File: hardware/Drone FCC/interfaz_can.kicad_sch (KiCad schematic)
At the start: 14 parts, among them J15 CAN 1 Connector 1, J16 CAN 2 Connector 1, U1 SN65HVD230, U2 SN65HVD230

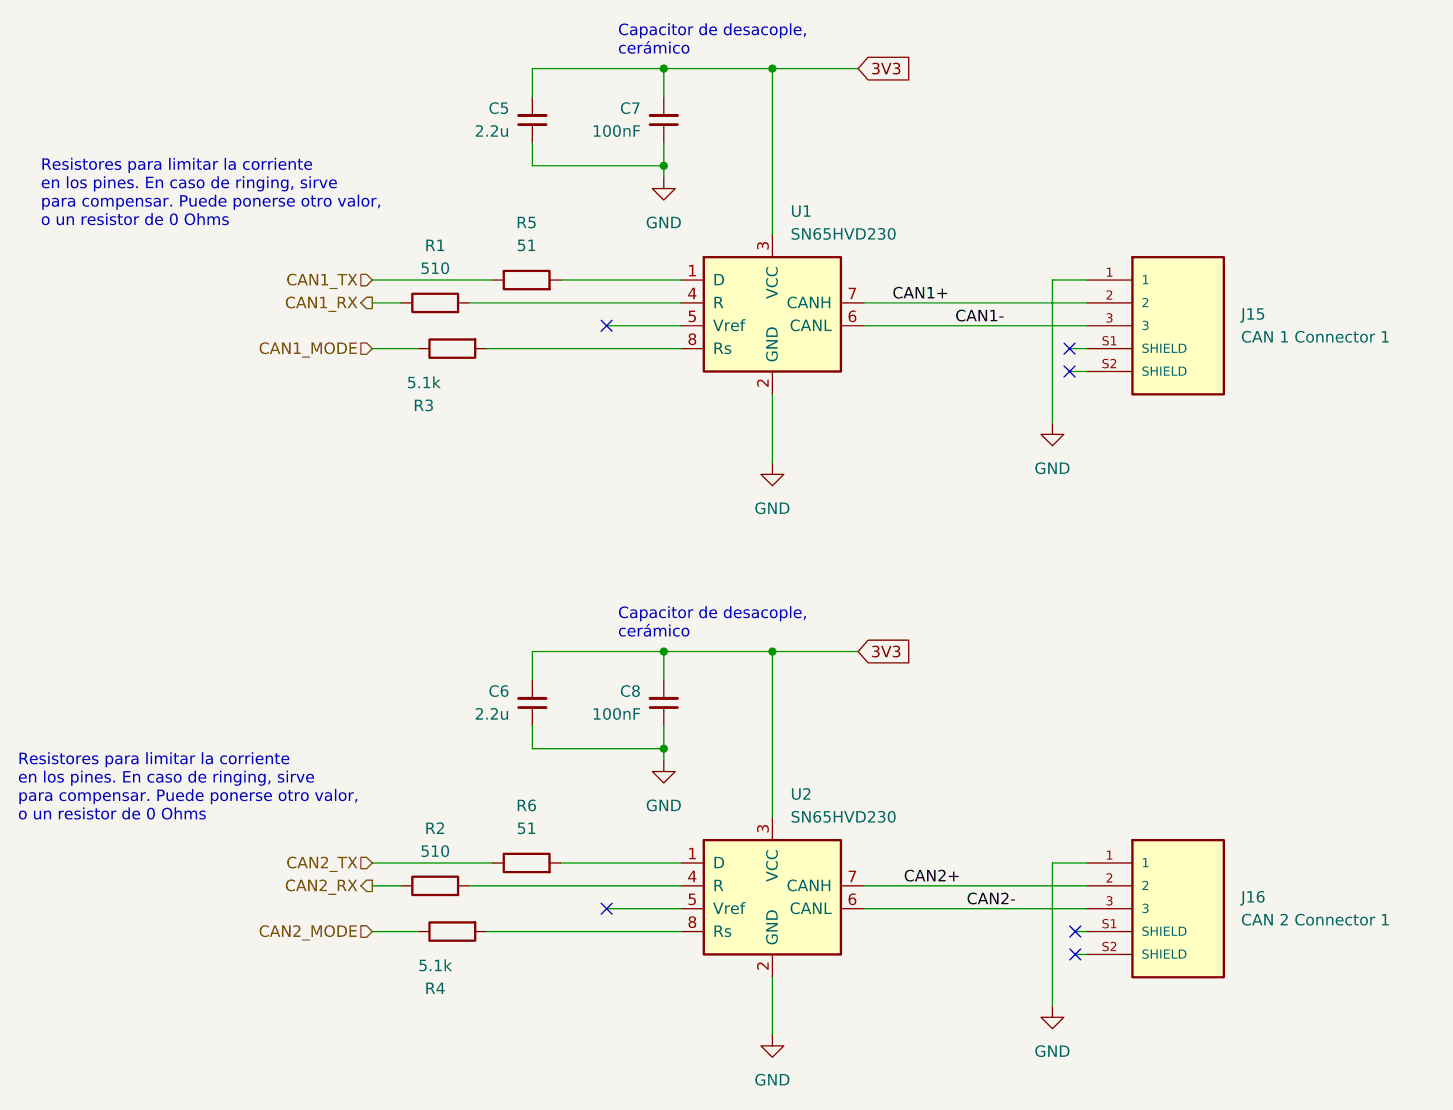
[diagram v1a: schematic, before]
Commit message: connected CAN transcievers slope control pin resistor to gnd
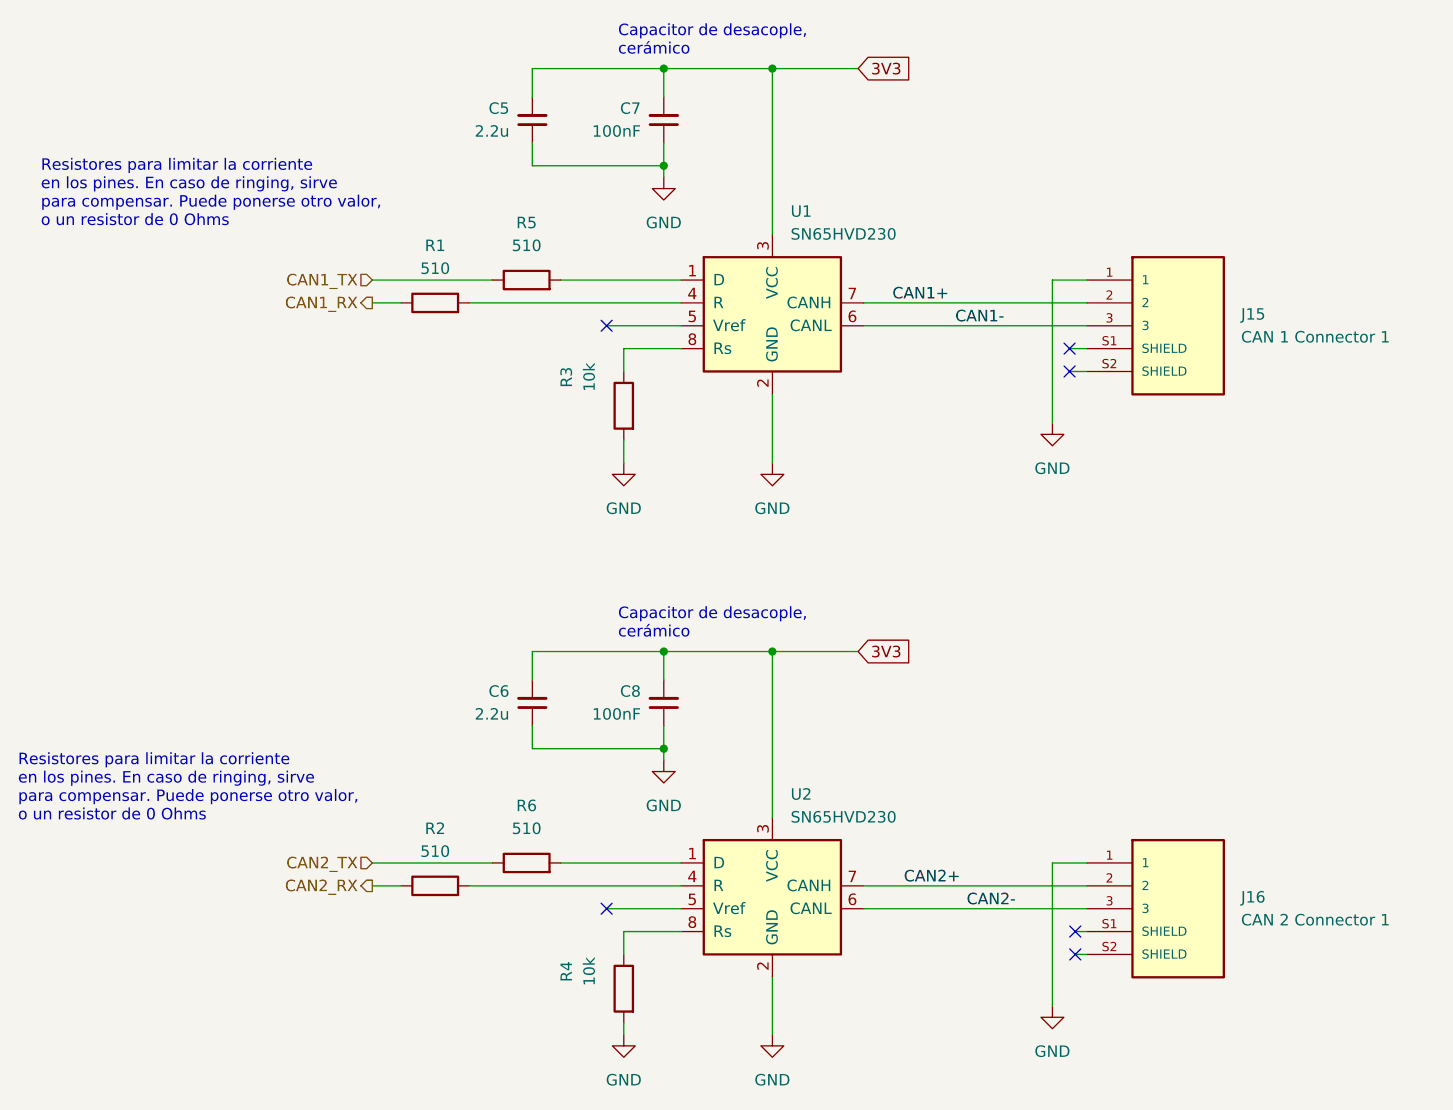
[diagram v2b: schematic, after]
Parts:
- R3, R4: value 5.1k -> 10k
- R5, R6: value 51 -> 510
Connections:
- net CAN1_MODE is gone; now on an unnamed net: R3.1
- net CAN2_MODE is gone; now on an unnamed net: R4.1
- net GND: now also R3.2, R4.2
- net at U1.8 (Rs): no longer R3.2
- net at U2.8 (Rs): no longer R4.2
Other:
- moved on the sheet: R3, R4
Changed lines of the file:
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@@
+    (stroke (width 0) (type default) (color 0 0 0 0))
+  )
+  (wire (pts (xy 128.905 57.15) (xy 135.255 57.15))
     (stroke (width 0) (type default) (color 0 0 0 0))
   )
@@
     (stroke (width 0) (type default) (color 0 0 0 0))
   )
-  (wire (pts (xy 100.965 121.92) (xy 106.045 121.92))
-    (stroke (width 0) (type default) (color 0 0 0 0))
-  )
   (wire (pts (xy 178.435 57.15) (xy 180.34 57.15))
     (stroke (width 0) (type default) (color 0 0 0 0))
@@
     (stroke (width 0) (type default) (color 0 0 0 0))
   )
-  (wire (pts (xy 113.665 57.15) (xy 135.255 57.15))
-    (stroke (width 0) (type default) (color 0 0 0 0))
-  )
-  (wire (pts (xy 113.665 121.92) (xy 135.255 121.92))
-    (stroke (width 0) (type default) (color 0 0 0 0))
-  )
   (wire (pts (xy 155.575 116.84) (xy 180.34 116.84))
     (stroke (width 0) (type default) (color 0 0 0 0))
   )
+  (wire (pts (xy 128.905 67.31) (xy 128.905 69.85))
+    (stroke (width 0) (type default) (color 0 0 0 0))
+  )
   (wire (pts (xy 155.575 54.61) (xy 180.34 54.61))
     (stroke (width 0) (type default) (color 0 0 0 0))
@@
     (stroke (width 0) (type default) (color 0 0 0 0))
   )
-  (wire (pts (xy 100.965 57.15) (xy 106.045 57.15))
-    (stroke (width 0) (type default) (color 0 0 0 0))
-  )
   (wire (pts (xy 133.35 90.805) (xy 133.35 93.98))
     (stroke (width 0) (type default) (color 0 0 0 0))
@@
     (stroke (width 0) (type default) (color 0 0 0 0))
   )
+  (wire (pts (xy 135.255 121.92) (xy 128.905 121.92))
+    (stroke (width 0) (type default) (color 0 0 0 0))
+  )
   (wire (pts (xy 145.415 127) (xy 145.415 133.35))
     (stroke (width 0) (type default) (color 0 0 0 0))
@@
     (stroke (width 0) (type default) (color 0 0 0 0))
   )
+  (wire (pts (xy 128.905 57.15) (xy 128.905 59.69))
+    (stroke (width 0) (type default) (color 0 0 0 0))
+  )
   (wire (pts (xy 127 54.61) (xy 135.255 54.61))
     (stroke (width 0) (type default) (color 0 0 0 0))
@@
     (stroke (width 0) (type default) (color 0 0 0 0))
   )
+  (wire (pts (xy 128.905 132.08) (xy 128.905 133.35))
+    (stroke (width 0) (type default) (color 0 0 0 0))
+  )
   (wire (pts (xy 176.53 114.3) (xy 180.34 114.3))
     (stroke (width 0) (type default) (color 0 0 0 0))
@@
   )
   (wire (pts (xy 179.07 121.92) (xy 180.34 121.92))
+    (stroke (width 0) (type default) (color 0 0 0 0))
+  )
+  (wire (pts (xy 128.905 121.92) (xy 128.905 124.46))
     (stroke (width 0) (type default) (color 0 0 0 0))
   )
@@
     (effects (font (size 1.27 1.27)) (justify right))
   )
-  (hierarchical_label "CAN2_MODE" (shape input) (at 100.965 121.92 180)
-    (effects (font (size 1.27 1.27)) (justify right))
-  )
-  (hierarchical_label "CAN1_MODE" (shape input) (at 100.965 57.15 180)
-    (effects (font (size 1.27 1.27)) (justify right))
-  )
   (symbol (lib_id "Device:R") (at 118.11 114.3 90) (unit 1)
     (in_bom yes) (on_board yes) (fields_autoplaced)
     (property "Reference" "R6" (id 0) (at 118.11 107.95 90))
-    (property "Value" "51" (id 1) (at 118.11 110.49 90))
+    (property "Value" "510" (id 1) (at 118.11 110.49 90))
     (property "Footprint" "Resistor_SMD:R_0402_1005Metric_Pad0.72x0.64mm_HandSolder" (id 2) (at 118.11 116.078 90)
       (effects (font (size 1.27 1.27)) hide)
@@
     (pin "2")
   )
-  (symbol (lib_id "Device:R") (at 109.855 121.92 90) (mirror x) (unit 1)
+  (symbol (lib_id "Device:R") (at 128.905 128.27 0) (mirror y) (unit 1)
     (in_bom yes) (on_board yes)
-    (property "Reference" "R4" (id 0) (at 107.95 128.27 90))
-    (property "Value" "5.1k" (id 1) (at 107.95 125.73 90))
-    (property "Footprint" "Resistor_SMD:R_0402_1005Metric_Pad0.72x0.64mm_HandSolder" (id 2) (at 109.855 120.142 90)
-      (effects (font (size 1.27 1.27)) hide)
-    )
-    (property "Datasheet" "~" (id 3) (at 109.855 121.92 0)
+    (property "Reference" "R4" (id 0) (at 122.555 126.365 90))
+    (property "Value" "10k" (id 1) (at 125.095 126.365 90))
+    (property "Footprint" "Resistor_SMD:R_0402_1005Metric_Pad0.72x0.64mm_HandSolder" (id 2) (at 130.683 128.27 90)
+      (effects (font (size 1.27 1.27)) hide)
+    )
+    (property "Datasheet" "~" (id 3) (at 128.905 128.27 0)
       (effects (font (size 1.27 1.27)) hide)
     )
@@
     (pin "2")
   )
-  (symbol (lib_id "Device:R") (at 109.855 57.15 90) (mirror x) (unit 1)
+  (symbol (lib_id "power:GND") (at 128.905 69.85 0) (unit 1)
+    (in_bom yes) (on_board yes) (fields_autoplaced)
+    (property "Reference" "#PWR0102" (id 0) (at 128.905 76.2 0)
+      (effects (font (size 1.27 1.27)) hide)
+    )
+    (property "Value" "GND" (id 1) (at 128.905 74.93 0))
+    (property "Footprint" "" (id 2) (at 128.905 69.85 0)
+      (effects (font (size 1.27 1.27)) hide)
+    )
+    (property "Datasheet" "" (id 3) (at 128.905 69.85 0)
+      (effects (font (size 1.27 1.27)) hide)
+    )
+    (pin "1")
+  )
+  (symbol (lib_id "Device:R") (at 128.905 63.5 0) (mirror y) (unit 1)
     (in_bom yes) (on_board yes)
-    (property "Reference" "R3" (id 0) (at 106.68 63.5 90))
-    (property "Value" "5.1k" (id 1) (at 106.68 60.96 90))
-    (property "Footprint" "Resistor_SMD:R_0402_1005Metric_Pad0.72x0.64mm_HandSolder" (id 2) (at 109.855 55.372 90)
-      (effects (font (size 1.27 1.27)) hide)
-    )
-    (property "Datasheet" "~" (id 3) (at 109.855 57.15 0)
+    (property "Reference" "R3" (id 0) (at 122.555 60.325 90))
+    (property "Value" "10k" (id 1) (at 125.095 60.325 90))
+    (property "Footprint" "Resistor_SMD:R_0402_1005Metric_Pad0.72x0.64mm_HandSolder" (id 2) (at 130.683 63.5 90)
+      (effects (font (size 1.27 1.27)) hide)
+    )
+    (property "Datasheet" "~" (id 3) (at 128.905 63.5 0)
       (effects (font (size 1.27 1.27)) hide)
     )
@@
     (pin "2")
   )
+  (symbol (lib_id "power:GND") (at 128.905 133.35 0) (unit 1)
+    (in_bom yes) (on_board yes) (fields_autoplaced)
+    (property "Reference" "#PWR0101" (id 0) (at 128.905 139.7 0)
+      (effects (font (size 1.27 1.27)) hide)
+    )
+    (property "Value" "GND" (id 1) (at 128.905 138.43 0))
+    (property "Footprint" "" (id 2) (at 128.905 133.35 0)
+      (effects (font (size 1.27 1.27)) hide)
+    )
+    (property "Datasheet" "" (id 3) (at 128.905 133.35 0)
+      (effects (font (size 1.27 1.27)) hide)
+    )
+    (pin "1")
+  )
   (symbol (lib_id "power:GND") (at 145.415 69.85 0) (unit 1)
     (in_bom yes) (on_board yes) (fields_autoplaced)
@@
     (in_bom yes) (on_board yes) (fields_autoplaced)
     (property "Reference" "R5" (id 0) (at 118.11 43.18 90))
-    (property "Value" "51" (id 1) (at 118.11 45.72 90))
+    (property "Value" "510" (id 1) (at 118.11 45.72 90))
     (property "Footprint" "Resistor_SMD:R_0402_1005Metric_Pad0.72x0.64mm_HandSolder" (id 2) (at 118.11 51.308 90)
       (effects (font (size 1.27 1.27)) hide)

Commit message: updated BOM with passive components
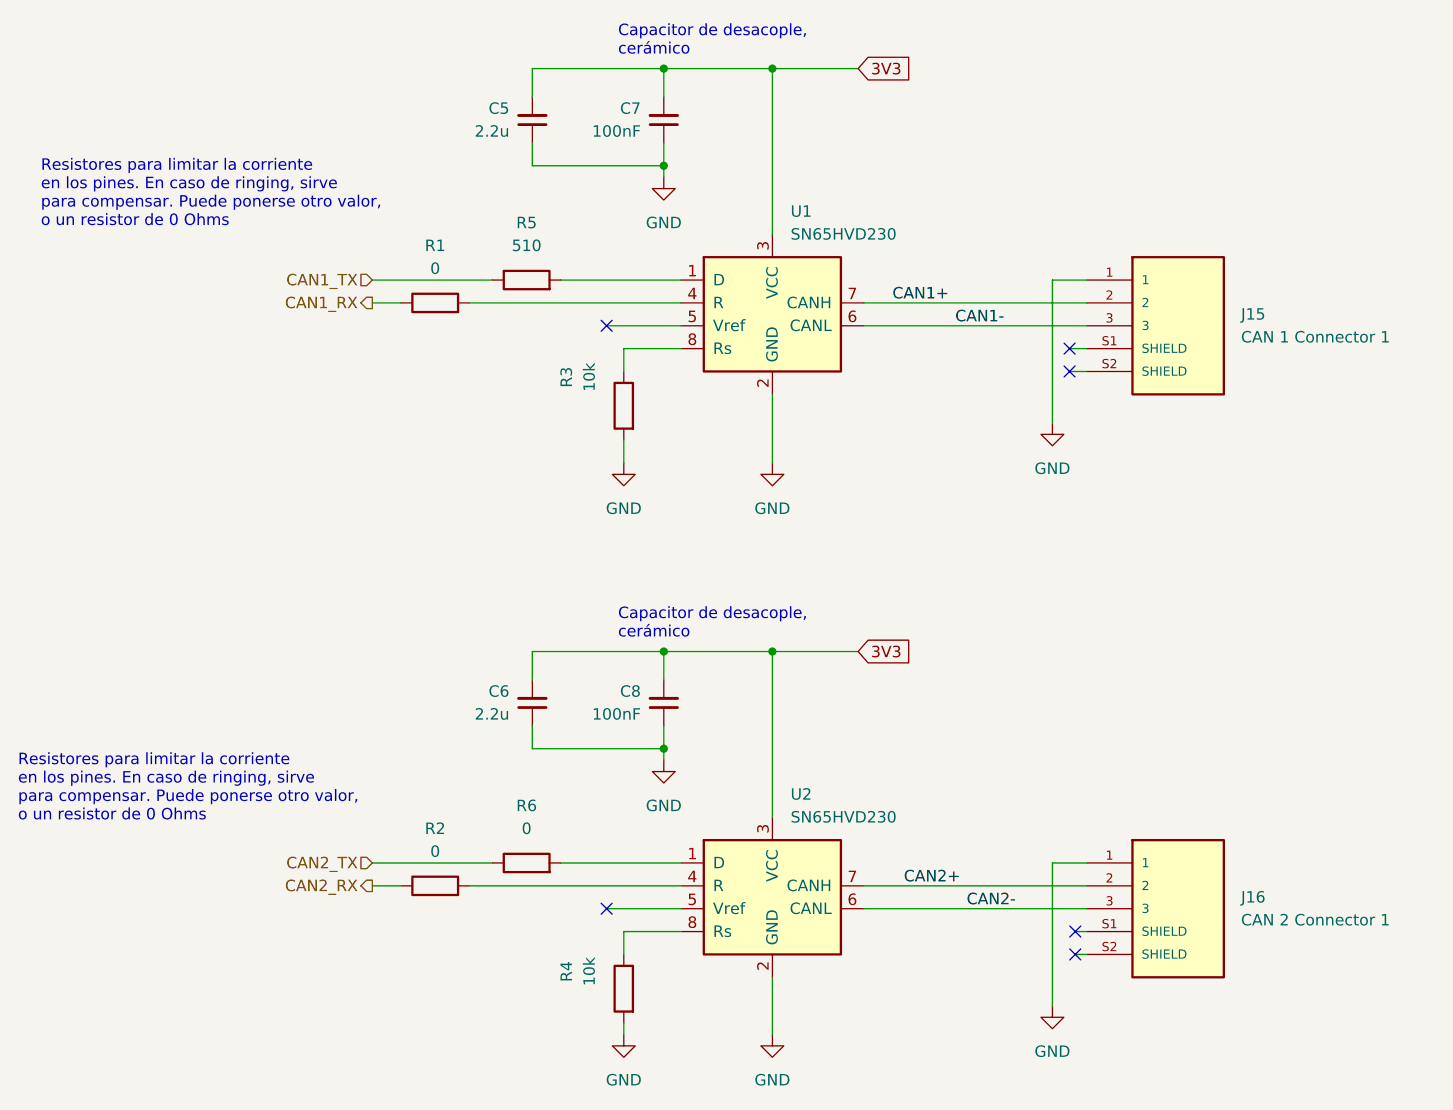
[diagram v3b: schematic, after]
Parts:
- R1, R2, R6: value 510 -> 0
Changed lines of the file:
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@@
     (in_bom yes) (on_board yes) (fields_autoplaced)
     (property "Reference" "R6" (id 0) (at 118.11 107.95 90))
-    (property "Value" "510" (id 1) (at 118.11 110.49 90))
+    (property "Value" "0" (id 1) (at 118.11 110.49 90))
     (property "Footprint" "Resistor_SMD:R_0402_1005Metric_Pad0.72x0.64mm_HandSolder" (id 2) (at 118.11 116.078 90)
       (effects (font (size 1.27 1.27)) hide)
@@
     (in_bom yes) (on_board yes) (fields_autoplaced)
     (property "Reference" "R1" (id 0) (at 107.95 45.72 90))
-    (property "Value" "510" (id 1) (at 107.95 48.26 90))
+    (property "Value" "0" (id 1) (at 107.95 48.26 90))
     (property "Footprint" "Resistor_SMD:R_0402_1005Metric_Pad0.72x0.64mm_HandSolder" (id 2) (at 107.95 53.848 90)
       (effects (font (size 1.27 1.27)) hide)
@@
     (in_bom yes) (on_board yes) (fields_autoplaced)
     (property "Reference" "R2" (id 0) (at 107.95 110.49 90))
-    (property "Value" "510" (id 1) (at 107.95 113.03 90))
+    (property "Value" "0" (id 1) (at 107.95 113.03 90))
     (property "Footprint" "Resistor_SMD:R_0402_1005Metric_Pad0.72x0.64mm_HandSolder" (id 2) (at 107.95 118.618 90)
       (effects (font (size 1.27 1.27)) hide)
